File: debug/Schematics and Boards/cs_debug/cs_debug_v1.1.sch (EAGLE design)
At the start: 241 parts, among them J1 J-JTAG-CORTEX_SMD, J19 Solar, J2 J-JTAG-CORTEX_SMD, J3 J-JTAG-CORTEX-NEEDLE6-LEGS, J4 J-SERIAL-PORT, J5 J-WURTH-USBC, Q10 2N7002P, Q3 FDN340P, Q4 2N7002P, Q5 FDN340P, Q6 2N7002P, Q7 FDN340P, Q8 2N7002P, Q9 FDN340P, U1 AP2120N-3.3TRG1, U10 OPA357AIDBVTG4, U11 DAC7574IDGS, U12 MCP73871T-2CCI/ML, U13 USB2412-DZK, U14 INA225AIDGK, U15 OPA357AIDBVTG4, U2 TLV1117LV33DCYR, U5 INA225AIDGK, U6 OPA357AIDBVTG4, U7 INA225AIDGK, U8 OPA357AIDBVTG4, U9 INA225AIDGK, Y1 EPSON_TSX-3225_24.0000MF10Z-C3, Y101 32.768kHz, Y102 12mHz-12pF-K7

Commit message: Schematic updates and component placement for debug placement
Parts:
- removed J.USB.DBG, J.USB.MN: USBABSMTDIP, ZX62D-AB-5P8:USBABSMTDIP
- removed J2: J-JTAG-CORTEX_SMD, Connectors:J-JTAG-CORTEX_SMD
- removed JP.HUB.VDD, JP.IP.CORE, JP.IP.RST, JP.UART.RX.IP, JP.UART.TX.IP, JP.USB.USART, JP.USBC.VBUS: JUMPER-SMT_2_NC_PASTE_NO-SILK, Connectors:JUMPER-SMT_2_NC_PASTE_NO-SILK
- removed JP.USB.DBG, JP.USBC: JUMPER-SMT_2_NO_PASTEFREE, Connectors:JUMPER-SMT_2_NO_PASTEFREE
- removed JP.USB.DDN, JP.USB.DDP, JP.USB.MDN, JP.USB.MDP, JP.USB.VBUSP, JP.VREG.SEL: JUMPER-SMT_3_1-NC_PASTE_NO-SILK, Connectors:JUMPER-SMT_3_1-NC_PASTE_NO-SILK
- removed J_DBG_TO_MAIN_HDR: HIROSE-DF40_30-PIN_CONNECTORS-HEADER, Connectors:HIROSE-DF40_30-PIN_CONNECTORS-HEADER
- removed L2: DLP11SN900HL2L, Inductors:DLP11SN900HL2L
- removed M.D.DA.VO, M.D.OA.EN, M.D.OA.N, M.D.OA.P, M.D.OA.VO, M.D.SDN, M.D.VN, M.D.VOI, M.P.DA.VO, M.P.OA.EN, M.P.OA.N, M.P.OA.P, M.P.OA.VO, M.P.SDN, M.P.VN, M.P.VOI, M.S.DA.VO, M.S.OA.EN, M.S.OA.N, M.S.OA.P, M.S.OA.VO, M.S.SDN, M.S.VN, M.S.VOI, M.T.DA.VO, M.T.OA.EN, M.T.OA.N, M.T.OA.P, M.T.OA.VO, M.T.SDN, M.T.VN, M.T.VOI: TPTP10SQ, TestPoints:TPTP10SQ
- removed R44, R45, R51, R52: 10k, Resistors:R-0402
- removed R50: 100k, Resistors:R-0402
- removed VR1, VR2, VR5, VR6, VR7, VR8: VARISTOR, Diodes:VARISTOR
- added C4, C5, C6: 0.1u, Capacitors:C-0402
- added C57: 1u, Capacitors:C-0402
- added CHRG, HUB.VDD, USB.VSRC: JUMPER-SMT_2_NC_PASTE_NO-SILK, Connectors:JUMPER-SMT_2_NC_PASTE_NO-SILK
- added D0DAO, D0OFF, D0OPN, D0OPO, D0OPP, D1DAO, D1OFF, D1OPN, D1OPO, D1OPP, PDAO, POPN, POPO, POPP, PROFF, SDAO, SOPN, SOPO, SOPP, STOFF: TPSTP10SQ, TestPoints:TPSTP10SQ
- added HUB.HS, HUB.SUSP, LOW_BAT, PG, STAT2: (no value), Diodes:LEDCHIPLED_0603
- added JP1: (no value), Connectors:J-HEADER-1X12
- added R10: 270, Resistors:R-0402
- added R9: 750, Resistors:R-0402
- added U204: LOADSWITCH-MIC94164, Switches:LOADSWITCH-MIC94164
- added U3: ESD122DMYR, Diodes:ESD122DMYR
- added VREG.SEL: JUMPER-SMT_3_1-NC_PASTE_NO-SILK, Connectors:JUMPER-SMT_3_1-NC_PASTE_NO-SILK
- C10, C13, C7: value 270nF -> 0.1u; device Capacitors:C-0603 -> Capacitors:C-0402; MPN C0603C274K8PACTU -> C0402C104K4RAC7411; PART_NO C0603C274K8PACTU -> C0402C104K4RAC7411; TC X5R -> (none)
- C20: value 270nF -> 10u; device Capacitors:C-0603 -> Capacitors:C-1206; MPN C0603C274K8PACTU -> C1206C476M8PACTU; PART_NO C0603C274K8PACTU -> C1206C476M8PACTU; TOL 0.5pF -> 20%
- D2: value BGX50A -> MBR120VLSFT3GOSCT-ND; device Diodes:BGX50A -> adafruit:DIODESOD-123; MPN (none) -> MBR120VLSFT3G; PART_NO (none) -> MBR120VLSFT3G
- J3: value J-JTAG-CORTEX-NEEDLE6-LEGS -> HIROSE-DF40_50-PIN_CONNECTORS-HEADER; device Connectors:J-JTAG-CORTEX-NEEDLE6-LEGS -> Connectors:HIROSE-DF40_50-PIN_CONNECTORS-HEADER
- JP.UART.VCC: value JUMPER-SMT_2_NC_PASTE_NO-SILK -> JUMPER-SMT_2_NO_PASTEFREE; device Connectors:JUMPER-SMT_2_NC_PASTE_NO-SILK -> Connectors:JUMPER-SMT_2_NO_PASTEFREE
- R2, R3: value 100k -> 1.5k; MPN ERJ-2GEJ104X -> ERJ-2GEJ152X; PART_NO ERJ-2GEJ104X -> ERJ-2GEJ152X
- R6: value 100k -> 1.15k; MPN ERJ-2GEJ104X -> ERJ-2RKF1151X; PART_NO ERJ-2GEJ104X -> ERJ-2RKF1151X; TOL (none) -> 1%
- R7: value 1M -> 100k; MPN ERJ-U02J105X -> ERJ-2GEJ104X; PART_NO ERJ-U02J105X -> ERJ-2GEJ104X
- S.ERASE, S.NRST: device Switches:SW_EVQ-P7L01P_SPST_RA -> Switches:MOMENTARY-SWITCH-SPST-SMD-5.2MM
- Y102: value 12mHz-12pF-K7 -> 12MHz-12pF-K7
- renumbered 3V3.IPROC to IP.3V3, JP.CHRG.MAIN to MN.CHRG, JP.EN.VMEAS to REGMEAS, JP.EN.VPROC to REGPROC, JP.EXT.PWR to EXT.SRC, JP.IP.ANA to IP.ANA, JP.IP.AREF to IP.AREF, JP.IP.OUT to IP.OUT, JP.IP.PLL to IP.PLL, JP.IP.UTMI to IP.UTMI, JP.IP.VDDIO to IP.VDDIO, JP.P.DTR to VP.DTR0, JP.P.PROC to VP.PRC, JP.P.STOR to VP.DTR1, JP.P.TEMP to VP.STOR, JP.UART.RX to MN.UART.RX, JP.UART.TX to MN.UART.TX, JP.VDD.MAIN to MN.VDD
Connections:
- net CM_DIFFAMP_N2 renamed CM_DTR1_DIFFAMP_N
- net CM_DIFFAMP_P2 renamed CM_DTR1_DIFFAMP_P
- net CM_DTR_DIFFAMP_GAIN0 renamed CM_DTR0_DIFFAMP_GAIN0
- net CM_DTR_DIFFAMP_GAIN1 renamed CM_DTR0_DIFFAMP_GAIN1
- net CM_DTR_V_SENSE_P renamed CM_DTR0_V_SENSE_P
- net CM_STORAGE_DIFFAMP_GAIN0 renamed CM_DTR1_DIFFAMP_GAIN0
- net CM_STORAGE_DIFFAMP_GAIN1 renamed CM_DTR1_DIFFAMP_GAIN1
- net CM_STORAGE_V_SENSE_P renamed CM_DTR1_V_SENSE_P
- net CM_TEMP_DIFFAMP_GAIN0 renamed CM_STOR_DIFFAMP_GAIN0
- net CM_TEMP_DIFFAMP_GAIN1 renamed CM_STOR_DIFFAMP_GAIN1
- net CM_TEMP_V_SENSE_P renamed CM_STOR_V_SENSE_P
- removed net CM_DIFFAMP_N1: C20.1, R58.2, U14.IN-
- removed net CM_DIFFAMP_N3: C10.1, R31.2, U7.IN-
- removed net CM_DIFFAMP_P1: C20.2, R59.2, U14.IN+
- removed net CM_DIFFAMP_P3: C10.2, R32.2, U7.IN+
- removed net CM_DTR_DCBIAS_SHUTDOWN: M.D.SDN.TP, Q8.GATE, R30.1, U_INSTR_PROC.PD2
- removed net CM_DTR_DIFFAMP_OUT: M.D.DA.VO.TP, U7.OUT, U_INSTR_PROC.PA6
- removed net CM_DTR_V_OFFSET_IN: M.D.VOI.TP, R25.1, U11.VOUTB
- removed net CM_DTR_V_SENSE_N: J_DBG_TO_MAIN_HDR.16, M.D.VN.TP, Q7.D, R26.1
- removed net CM_OPAMP_ENABLE1: M.T.OA.EN.TP, Q10.DRAIN, Q9.G, R54.1, U15.ENABLE
- removed net CM_OPAMP_ENABLE2: M.S.OA.EN.TP, Q5.G, Q6.DRAIN, R34.1, U10.ENABLE
- removed net CM_OPAMP_ENABLE3: M.D.OA.EN.TP, Q7.G, Q8.DRAIN, R27.1, U8.ENABLE
- removed net CM_OPAMP_N1: M.T.OA.N.TP, R55.1, R56.2, U15.IN-
- removed net CM_OPAMP_N2: M.S.OA.N.TP, R35.1, R36.2, U10.IN-
- removed net CM_OPAMP_N3: M.D.OA.N.TP, R28.1, R29.2, U8.IN-
- removed net CM_OPAMP_OUT1: M.T.OA.VO.TP, Q9.S, R55.2, R58.1, U15.OUT
- removed net CM_OPAMP_OUT2: M.S.OA.VO.TP, Q5.S, R35.2, R38.1, U10.OUT
- removed net CM_OPAMP_OUT3: M.D.OA.VO.TP, Q7.S, R28.2, R31.1, U8.OUT
- removed net CM_OPAMP_P2: M.S.OA.P.TP, R24.2, R33.2, U10.IN+
- removed net CM_STORAGE_DCBIAS_SHUTDOWN: M.S.SDN.TP, Q6.GATE, R37.1, U_INSTR_PROC.PD1
- removed net CM_STORAGE_DIFFAMP_OUT: M.S.DA.VO.TP, U9.OUT, U_INSTR_PROC.PA4
- removed net CM_STORAGE_V_OFFSET_IN: M.S.VOI.TP, R24.1, U11.VOUTC
- removed net CM_STORAGE_V_SENSE_N: J_DBG_TO_MAIN_HDR.18, M.S.VN.TP, Q5.D, R33.1
- removed net CM_TEMP_DCBIAS_SHUTDOWN: M.T.SDN.TP, Q10.GATE, R57.1, U_INSTR_PROC.PD0
- removed net CM_TEMP_DIFFAMP_OUT: M.T.DA.VO.TP, U14.OUT, U_INSTR_PROC.PA3
- removed net CM_TEMP_V_OFFSET_IN: M.T.VOI.TP, R40.1, U11.VOUTD
- removed net CM_TEMP_V_SENSE_N: J_DBG_TO_MAIN_HDR.20, M.T.VN.TP, Q9.D, R53.1
- removed net HUB_INSTR_PROC_USB_D_N: JP.USB.DDN.3, U13.USBDM_DN2
- removed net HUB_INSTR_PROC_USB_D_P: JP.USB.DDP.3, U13.USBDP_DN2
- removed net HUB_MAIN_USB_DATA_N: JP.USB.MDN.3, U13.USBDM_DN1
- removed net HUB_MAIN_USB_DATA_P: JP.USB.MDP.3, U13.USBDP_DN1
- removed net INSTR_PROC_JTAG_TCK/SWCLK: J2.SWDCLK/TCK, J3.SWCLK, R3.1, U_INSTR_PROC.PB28
- removed net INSTR_PROC_JTAG_TDI: J2.NC/TDI, R6.1, U_INSTR_PROC.PB29
- removed net INSTR_PROC_JTAG_TDO/SWO: J2.SWO/TDO, J3.SWO, U_INSTR_PROC.PB30
- removed net INSTR_PROC_JTAG_TMS/SWDIO: J2.SWDIO/TMS, J3.SWDIO, R2.1, U_INSTR_PROC.PB31
- removed net INSTR_PROC_NRESET: J2.!RESET, J3.NRESET, JP.IP.RST.1
- removed net MAIN_TRACE_CLK/GPIO4: J_DBG_TO_MAIN_HDR.26, U_INSTR_PROC.PC15
- removed net MAIN_TRACE_D0/GPIO6: J_DBG_TO_MAIN_HDR.23, U_INSTR_PROC.PB1
- removed net MAIN_TRACE_D1/GPIO7: J_DBG_TO_MAIN_HDR.25, U_INSTR_PROC.PB2
- removed net MAIN_TRACE_D2/GPIO8: J_DBG_TO_MAIN_HDR.27
- removed net MAIN_TRACE_D3/GPIO9: J_DBG_TO_MAIN_HDR.29
- removed net MAIN_TRACE_SWO/GPIO5: J_DBG_TO_MAIN_HDR.28, U_INSTR_PROC.PB0
- removed net USB_BKUP_DBG_D_N: J.USB.DBG.D-, JP.USB.DDN.1, VR5.1
- removed net USB_BKUP_DBG_D_P: J.USB.DBG.D+, JP.USB.DDP.1, VR2.1
- removed net USB_BKUP_DBG_OTGID: J.USB.DBG.USBID, VR1.1
- removed net USB_BKUP_DBG_VBUS: J.USB.DBG.VBUS, JP.USB.DBG.2, JP.USB.VBUSP.1
- removed net USB_BKUP_MAIN_D_N: J.USB.MN.D-, JP.USB.MDP.1, VR8.1
- removed net USB_BKUP_MAIN_D_P: J.USB.MN.D+, JP.USB.MDN.1, VR7.1
- removed net USB_BKUP_MAIN_OTGID: J.USB.MN.USBID, VR6.1
- removed net USB_BKUP_MAIN_VBUS: J.USB.MN.VBUS, JP.USBC.2
- removed net USB_CONN_D_N: D2.AC1, J5_CONNECTOR.DP1, J5_CONNECTOR.DP2, L2.3, VR3.1
- removed net USB_CONN_D_P: D2.AC2, J5_CONNECTOR.DN1, J5_CONNECTOR.DN2, L2.2, VR4.1
- removed net VDDOUT_1: JP.IP.CORE.1, U_INSTR_PROC.VDDCORE1, U_INSTR_PROC.VDDCORE2, U_INSTR_PROC.VDDCORE3, U_INSTR_PROC.VDDCORE4, U_INSTR_PROC.VDDCORE5
- new net +3V3_INSTR_PROC: HUB.VDD.1
- new net CM_DTR0_DCBIAS_SHUTDOWN: Q8.GATE, R30.1, U_INSTR_PROC.PD2
- new net CM_DTR0_DIFFAMP_N: C7.1, R31.2, U7.IN-
- new net CM_DTR0_DIFFAMP_OUT: D0DAO.PP, U7.OUT, U_INSTR_PROC.PA6
- new net CM_DTR0_DIFFAMP_P3: C7.2, R32.2, U7.IN+
- new net CM_DTR0_OPAMP_ENABLE: Q7.G, Q8.DRAIN, R27.1, U8.ENABLE
- new net CM_DTR0_OPAMP_N: D0OPN.PP, R28.1, R29.2, U8.IN-
- new net CM_DTR0_OPAMP_OUT: D0OPO.PP, Q7.S, R28.2, R31.1, U8.OUT
- new net CM_DTR0_V_OFFSET_IN: D0OFF.PP, R25.1, U11.VOUTB
- new net CM_DTR0_V_SENSE_N: J3.18, Q7.D, R26.1
- new net CM_DTR1_DCBIAS_SHUTDOWN: Q6.GATE, R37.1, U_INSTR_PROC.PD1
- new net CM_DTR1_DIFFAMP_OUT: D1DAO.PP, U9.OUT, U_INSTR_PROC.PA4
- new net CM_DTR1_OPAMP_N: D1OPN.PP, R35.1, R36.2, U10.IN-
- new net CM_DTR1_OPAMP_OUT: D1OPO.PP, Q5.S, R35.2, R38.1, U10.OUT
- new net CM_DTR1_OPAMP_P: D1OPP.PP, R24.2, R33.2, U10.IN+
- new net CM_DTR1_V_OFFSET_IN: D1OFF.PP, R24.1, U11.VOUTC
- new net CM_DTR1_V_SENSE_N: J3.20, Q5.D, R33.1
- new net CM_DTR_OPAMP_ENABLE: Q5.G, Q6.DRAIN, R34.1, U10.ENABLE
- new net CM_STORV_SENSE_N: J3.22
- new net CM_STOR_DCBIAS_SHUTDOWN: Q10.GATE, R57.1, U_INSTR_PROC.PD0
- new net CM_STOR_DIFFAMP_N1: C10.1, R58.2, U14.IN-
- new net CM_STOR_DIFFAMP_OUT: SDAO.PP, U14.OUT, U_INSTR_PROC.PA3
- new net CM_STOR_DIFFAMP_P1: C10.2, R59.2, U14.IN+
- new net CM_STOR_OPAMP_ENABLE: Q10.DRAIN, Q9.G, R54.1, U15.ENABLE
- new net CM_STOR_OPAMP_N: R55.1, R56.2, SOPN.PP, U15.IN-
- new net CM_STOR_OPAMP_OUT: Q9.S, R55.2, R58.1, SOPO.PP, U15.OUT
- new net CM_STOR_V_OFFSET_IN: R40.1, STOFF.PP, U11.VOUTD
- new net CM_STOR_V_SENSE_N: Q9.D, R53.1
- new net MAIN_GPIO10: J3.40, U_INSTR_PROC.PB1
- new net MAIN_GPIO11: J3.38, U_INSTR_PROC.PB2
- new net MAIN_GPIO4/SERCOM_P0: J3.30, JP1.2
- new net MAIN_GPIO5/SERCOM_P1: J3.32, JP1.3
- new net MAIN_GPIO6/SERCOM_P2: J3.34, JP1.4
- new net MAIN_GPIO7/SERCOM_P3: J3.36, JP1.5
- new net MAIN_GPIO8: J3.44, U_INSTR_PROC.PC15
- new net MAIN_GPIO9: J3.42, U_INSTR_PROC.PB0
- new net MAIN_TRACE_CLK/GPIO17: J3.23, JP1.11
- new net MAIN_TRACE_D0/GPIO13: J3.15, JP1.7
- new net MAIN_TRACE_D1/GPIO14: J3.17, JP1.8
- new net MAIN_TRACE_D2/GPIO15: J3.19, JP1.9
- new net MAIN_TRACE_D3/GPIO16: J3.21, JP1.10
- new net MAIN_TRACE_SWO/GPIO12: J3.13, JP1.6
- new net N$12: R2.1, U12.STAT1/!LBO
- new net N$17: C5.1, U13.PLLFILT
- new net N$18: R3.2, STAT2.C
- new net N$19: PG.C, R6.2
- new net N$20: R6.1, U12.!PG
- new net N$22: HUB.SUSP.A, R9.1
- new net N$23: HUB.HS.A, R10.1
- new net N$24: CHRG.1, R201.2, U12.!TE, U12.CE, U12.IN, U12.PROG2, U12.SEL
- new net VUSB_DIODE: D2.C, USB.VSRC.1
- net 3V3_INSTR_MEAS: now also JP1.1
- net 3V3_INSTR_PROC: no longer C49.1, C50.1, C51.1, C52.1, C53.1, C54.1, J2.VCC, J3.VTREF, JP.HUB.VDD.1, R2.2, R3.2, R44.2, R45.2, R51.2, R52.2, R6.2
- net CM_DIFFAMP_N4: now also C6.1; no longer C7.1
- net CM_DIFFAMP_P4: now also C6.2; no longer C7.2
- net CM_OPAMP_ENABLE4: no longer M.P.OA.EN.TP
- net CM_OPAMP_N4: now also POPN.PP; no longer M.P.OA.N.TP
- net CM_OPAMP_OUT4: now also POPO.PP; no longer M.P.OA.VO.TP
- net CM_OPAMP_P1: now also SOPP.PP; no longer M.T.OA.P.TP
- net CM_OPAMP_P3: now also D0OPP.PP; no longer M.D.OA.P.TP
- net CM_OPAMP_P4: now also POPP.PP; no longer M.P.OA.P.TP
- net CM_PROC_DCBIAS_SHUTDOWN: no longer M.P.SDN.TP
- net CM_PROC_DIFFAMP_OUT: now also PDAO.PP; no longer M.P.DA.VO.TP
- net CM_PROC_V_OFFSET_IN: now also PROFF.PP; no longer M.P.VOI.TP
- net CM_PROC_V_SENSE_N: now also J3.16; no longer J_DBG_TO_MAIN_HDR.14, M.P.VN.TP
- net DGND: now also C20.2, C4.2, C5.2, C57.2, HUB.HS.C, HUB.SUSP.C, J3.1, J3.3, J3.5, J3.7, JP1.12, R7.1, U204.GND, U3.GND; no longer D2.-, J.USB.DBG.GND, J.USB.DBG.SHIELD, J.USB.MN.GND, J.USB.MN.SHIELD, J2.GND@3, J2.GND@5, J2.GNDDTCT, J3.GND, J_DBG_TO_MAIN_HDR.1, J_DBG_TO_MAIN_HDR.3, J_DBG_TO_MAIN_HDR.5, R50.1, VR1.2, VR2.2, VR5.2, VR6.2, VR7.2, VR8.2
- net INSTR_PROC_NRESET_SW: no longer JP.IP.RST.2
- net INSTR_PROC_USB_D_N: now also U13.USBDM_DN1; no longer JP.USB.DDN.2
- net INSTR_PROC_USB_D_P: now also U13.USBDP_DN1; no longer JP.USB.DDP.2
- net MAIN_GPIO0: now also J3.31; no longer J_DBG_TO_MAIN_HDR.7
- net MAIN_GPIO1: now also J3.29; no longer J_DBG_TO_MAIN_HDR.9
- net MAIN_GPIO2: now also J3.27; no longer J_DBG_TO_MAIN_HDR.11
- net MAIN_GPIO3: now also J3.25; no longer J_DBG_TO_MAIN_HDR.13
- net MAIN_NRESET: now also J3.24; no longer J_DBG_TO_MAIN_HDR.30
- net MAIN_SWD_SWCLK: now also J3.28; no longer J_DBG_TO_MAIN_HDR.19
- net MAIN_SWD_SWDIO: now also J3.26; no longer J_DBG_TO_MAIN_HDR.21
- net MAIN_USART_RX: now also J3.9; no longer JP.UART.TX.IP.1, J_DBG_TO_MAIN_HDR.17
- net MAIN_USART_TX: now also J3.11; no longer JP.UART.RX.IP.1, JP.USB.USART.2, J_DBG_TO_MAIN_HDR.15
- net MAIN_USB_DATA_N: now also J3.49, U13.USBDM_DN2; no longer JP.USB.MDN.2, J_DBG_TO_MAIN_HDR.22
- net MAIN_USB_DATA_P: now also J3.47, U13.USBDP_DN2; no longer JP.USB.MDP.2, J_DBG_TO_MAIN_HDR.24
- net N$14: now also R3.1, U12.STAT2; no longer R45.1, U13.PRTPWR1
- net N$16: now also C4.1, U13.CRFILT; no longer R44.1, U13.PRTPWR2
- net N$3: now also S201.P, U204.ENABLE; no longer JP.UART.TX.IP.2, U_INSTR_PROC.PD5
- net N$5: now also LOW_BAT.C, R2.2; no longer JP.UART.RX.IP.2, U_INSTR_PROC.PD4
- net N$6: now also C20.1, S201.S, U204.VIN; no longer S201.P
- net UCTX_DBGRX: no longer JP.USB.USART.1
- net USBC_VBUS: now also D2.A; no longer D2.+, JP.USB.VBUSP.3, JP.USBC.VBUS.1
- net USB_D_N: now also J5_CONNECTOR.DN1, J5_CONNECTOR.DN2, U3.IO2, VR3.1; no longer L2.4
- net USB_D_P: now also J5_CONNECTOR.DP1, J5_CONNECTOR.DP2, U3.IO1, VR4.1; no longer L2.1
- net USB_HS_IND: now also R10.2; no longer R50.2
- net USB_HUB_VDD: now also C49.1, C50.1, C51.1, C52.1, C53.1, C54.1, HUB.VDD.2; no longer JP.HUB.VDD.2
- net USB_NONRMV0: now also R9.2; no longer R51.1
- net USB_NONRMV1: now also R7.2; no longer R52.1
- net USB_VBUS_IPROC: no longer JP.USB.VBUSP.2
- net USB_XIN: no longer R7.2
- net USB_XOUT: no longer R7.1
- net VCHRG_OUT: now also VREG.SEL.3; no longer JP.VREG.SEL.3
- net VDDOUT: now also U_INSTR_PROC.VDDCORE1, U_INSTR_PROC.VDDCORE2, U_INSTR_PROC.VDDCORE3, U_INSTR_PROC.VDDCORE4, U_INSTR_PROC.VDDCORE5; no longer JP.IP.CORE.2
- net VDD_TO_MAIN: now also J3.2, J3.4, J3.6; no longer J_DBG_TO_MAIN_HDR.2, J_DBG_TO_MAIN_HDR.4
- net VREG_IN: now also VREG.SEL.2; no longer JP.VREG.SEL.2
- net VSRC: now also USB.VSRC.2; no longer JP.USB.DBG.1, JP.USBC.1, JP.USBC.VBUS.2
- net VSRC_RAW: now also C57.1, CHRG.2, LOW_BAT.A, PG.A, STAT2.A, U204.VOUT, VREG.SEL.1; no longer JP.VREG.SEL.1, R201.2, S201.S, U12.!TE, U12.CE, U12.IN, U12.PROG2, U12.SEL
- net V_BATT_MAIN: now also J3.10, J3.12, J3.8; no longer J_DBG_TO_MAIN_HDR.10, J_DBG_TO_MAIN_HDR.6, J_DBG_TO_MAIN_HDR.8
- net V_SENSE_P: now also J3.14; no longer J_DBG_TO_MAIN_HDR.12
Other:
- note added: "Daughter Board High-Side Current Monitor 0"
- note added: "Daughter High-Side Current Monitor 1"
- note added: "GPIO Expansion"
- note added: "Green"
- note added: "Orange"
- note added: "Red"
- note added: "Storage/FLASH High-Side Current Monitor"
- note added: "Yellow"
- note removed: "Add DLP11SN900SL2 and BGX50A"
- note removed: "Both debug connector options in case dev is missing a cable. Tag-connect is missing TDI, so it may not work"
- note removed: "Daughter Board High-Side Current Monitor"
- note removed: "Instrumentation Processor Debugging"
- note removed: "Storage High-Side Current Monitor"
- note removed: "Temp High-Side Current Monitor"
- note removed: "USB Micro Connectors (backup for hub)"
- moved on the sheet: C10, C208, C7, D1, L1, R48, R7, S201

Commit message: Finished schematic revision for main, debug boards.
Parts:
- C.PHAT: value 10u -> 47u
- renumbered C20 to C.PHAT, J4 to J.FTDI, R1 to R.GND, U_INSTR_PROC to U.IP
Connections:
- net N$3 renamed VREG.SW.EN
- net N$6 renamed VSRC_SW
- removed net USB_VBUS_IPROC: U.IP.VBUS
- net USBC_VBUS: now also U.IP.VBUS
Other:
- note added: "GPIO Expansion for main board"
- note added: "Monitor 0 is nominally for measuring current of the entire stack of daughter boards, but can be switched to instead measure the current of a particular component or subsystem."
- note removed: "Connection questionable"
- note removed: "GPIO Expansion"
- note removed: "pull-up for power pins; hub should not shutdown other devices"
- moved on the sheet: HUB.HS, JP1, PG, STAT2

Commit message: Route differential USB signals
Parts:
- added R1: 51k, Resistors:R-0402
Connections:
- removed net N$22: HUB.SUSP.A, R9.1
- new net N$3: HUB.SUSP.C, R9.1
- net 3V3_INSTR_PROC: now also HUB.SUSP.A, R1.1
- net DGND: no longer HUB.SUSP.C
- net USB_NONRMV0: now also R1.2
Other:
- note added: "Mark port 2 as removeable"
- moved on the sheet: C4, C5, HUB.SUSP, R48, R7, R9

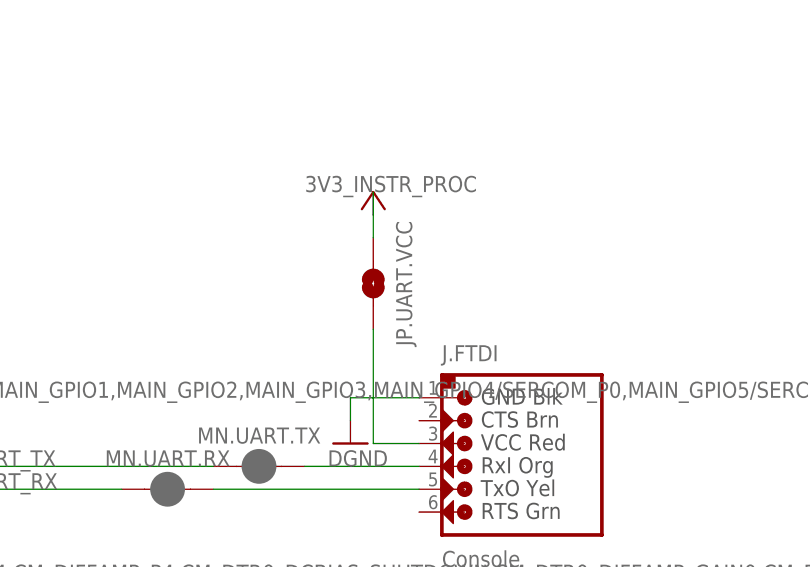
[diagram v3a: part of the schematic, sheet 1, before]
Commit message: Edit silk and documentation layers for pick-and-place assembly
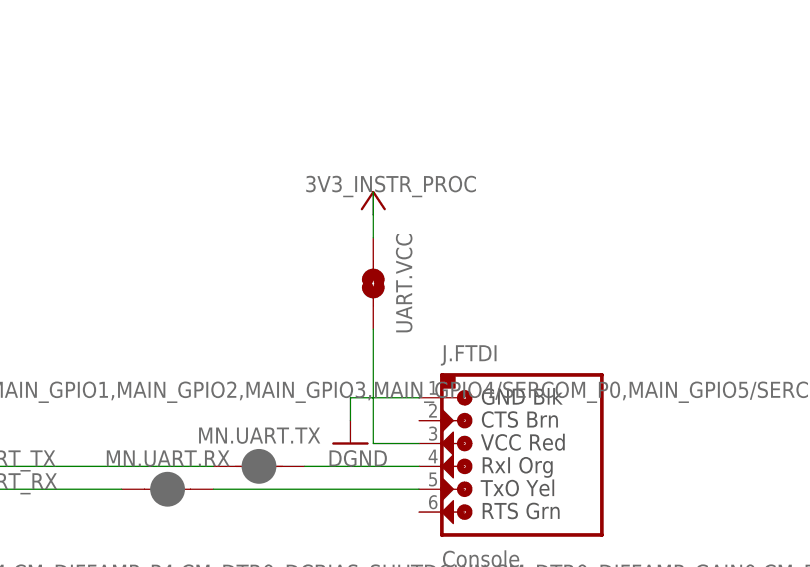
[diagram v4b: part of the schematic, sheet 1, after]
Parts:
- renumbered JP.UART.VCC to UART.VCC
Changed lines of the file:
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@@
 </part>
 <part name="SUPPLY25" library="Supplies" deviceset="+3V3" device=""/>
-<part name="JP.UART.VCC" library="Connectors" deviceset="JUMPER-SMT_2_NO_PASTEFREE" device=""/>
+<part name="UART.VCC" library="Connectors" deviceset="JUMPER-SMT_2_NO_PASTEFREE" device=""/>
 <part name="C46" library="Capacitors" deviceset="C-" device="0603" value="2.2uF">
 <attribute name="MPN" value="C0603C225K8RACTU"/>
@@
 </instance>
 <instance part="SUPPLY25" gate="G$1" x="523.24" y="236.22" smashed="yes"/>
-<instance part="JP.UART.VCC" gate="G$1" x="523.24" y="226.06" smashed="yes" rot="R270">
+<instance part="UART.VCC" gate="G$1" x="523.24" y="226.06" smashed="yes" rot="R270">
 <attribute name="NAME" x="525.78" y="226.06" size="1.778" layer="95" font="vector" rot="R270" align="bottom-center"/>
 </instance>
@@
 <label x="515.62" y="236.22" size="1.778" layer="95"/>
 <pinref part="SUPPLY25" gate="G$1" pin="+3V3"/>
-<pinref part="JP.UART.VCC" gate="G$1" pin="1"/>
+<pinref part="UART.VCC" gate="G$1" pin="1"/>
 <wire x1="523.24" y1="231.14" x2="523.24" y2="233.68" width="0.1524" layer="91"/>
 </segment>
@@
 <net name="N$11" class="0">
 <segment>
-<pinref part="JP.UART.VCC" gate="G$1" pin="2"/>
+<pinref part="UART.VCC" gate="G$1" pin="2"/>
 <pinref part="J.FTDI" gate="J$1" pin="VCC-I"/>
 <wire x1="523.24" y1="220.98" x2="523.24" y2="208.28" width="0.1524" layer="91"/>

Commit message: Route minimal analog signals under ground bridge, add near ground plugs
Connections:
- removed net CM_STORV_SENSE_N: J3.22
- net CM_STOR_V_SENSE_N: now also J3.22
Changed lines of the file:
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@@
 </instances>
 <busses>
-<bus name="POWER_SENSING:CM_DIFFAMP_N4,CM_DIFFAMP_P4,CM_DTR0_DCBIAS_SHUTDOWN,CM_DTR0_DIFFAMP_GAIN0,CM_DTR0_DIFFAMP_GAIN1,CM_DTR0_DIFFAMP_N,CM_DTR0_DIFFAMP_OUT,CM_DTR0_DIFFAMP_P3,CM_DTR0_OPAMP_ENABLE,CM_DTR0_OPAMP_N,CM_DTR0_OPAMP_OUT,CM_DTR0_V_OFFSET_IN,CM_DTR0_V_SENSE_N,CM_DTR0_V_SENSE_P,CM_DTR1_DCBIAS_SHUTDOWN,CM_DTR1_DIFFAMP_GAIN0,CM_DTR1_DIFFAMP_GAIN1,CM_DTR1_DIFFAMP_N,CM_DTR1_DIFFAMP_OUT,CM_DTR1_DIFFAMP_P,CM_DTR1_OPAMP_N,CM_DTR1_OPAMP_OUT,CM_DTR1_OPAMP_P,CM_DTR1_V_OFFSET_IN,CM_DTR1_V_SENSE_N,CM_DTR1_V_SENSE_P,CM_DTR_OPAMP_ENABLE,CM_OPAMP_ENABLE4,CM_OPAMP_N4,CM_OPAMP_OUT4,CM_OPAMP_P1,CM_OPAMP_P3,CM_OPAMP_P4,CM_PROC_DCBIAS_SHUTDOWN,CM_PROC_DIFFAMP_GAIN0,CM_PROC_DIFFAMP_GAIN1,CM_PROC_DIFFAMP_OUT,CM_PROC_V_OFFSET_IN,CM_PROC_V_SENSE_N,CM_PROC_V_SENSE_P,CM_STOR_DCBIAS_SHUTDOWN,CM_STOR_DIFFAMP_GAIN0,CM_STOR_DIFFAMP_GAIN1,CM_STOR_DIFFAMP_N1,CM_STOR_DIFFAMP_OUT,CM_STOR_DIFFAMP_P1,CM_STOR_OPAMP_ENABLE,CM_STOR_OPAMP_N,CM_STOR_OPAMP_OUT,CM_STOR_V_OFFSET_IN,CM_STORV_SENSE_N,CM_STOR_V_SENSE_N,CM_STOR_V_SENSE_P,V_SENSE_P">
+<bus name="POWER_SENSING:CM_DIFFAMP_N4,CM_DIFFAMP_P4,CM_DTR0_DCBIAS_SHUTDOWN,CM_DTR0_DIFFAMP_GAIN0,CM_DTR0_DIFFAMP_GAIN1,CM_DTR0_DIFFAMP_N,CM_DTR0_DIFFAMP_OUT,CM_DTR0_DIFFAMP_P3,CM_DTR0_OPAMP_ENABLE,CM_DTR0_OPAMP_N,CM_DTR0_OPAMP_OUT,CM_DTR0_V_OFFSET_IN,CM_DTR0_V_SENSE_N,CM_DTR0_V_SENSE_P,CM_DTR1_DCBIAS_SHUTDOWN,CM_DTR1_DIFFAMP_GAIN0,CM_DTR1_DIFFAMP_GAIN1,CM_DTR1_DIFFAMP_N,CM_DTR1_DIFFAMP_OUT,CM_DTR1_DIFFAMP_P,CM_DTR1_OPAMP_N,CM_DTR1_OPAMP_OUT,CM_DTR1_OPAMP_P,CM_DTR1_V_OFFSET_IN,CM_DTR1_V_SENSE_N,CM_DTR1_V_SENSE_P,CM_DTR_OPAMP_ENABLE,CM_OPAMP_ENABLE4,CM_OPAMP_N4,CM_OPAMP_OUT4,CM_OPAMP_P1,CM_OPAMP_P3,CM_OPAMP_P4,CM_PROC_DCBIAS_SHUTDOWN,CM_PROC_DIFFAMP_GAIN0,CM_PROC_DIFFAMP_GAIN1,CM_PROC_DIFFAMP_OUT,CM_PROC_V_OFFSET_IN,CM_PROC_V_SENSE_N,CM_PROC_V_SENSE_P,CM_STOR_DCBIAS_SHUTDOWN,CM_STOR_DIFFAMP_GAIN0,CM_STOR_DIFFAMP_GAIN1,CM_STOR_DIFFAMP_N1,CM_STOR_DIFFAMP_OUT,CM_STOR_DIFFAMP_P1,CM_STOR_OPAMP_ENABLE,CM_STOR_OPAMP_N,CM_STOR_OPAMP_OUT,CM_STOR_V_OFFSET_IN,CM_STOR_V_SENSE_N,CM_STOR_V_SENSE_P,V_SENSE_P">
 <segment>
 <wire x1="137.16" y1="172.72" x2="137.16" y2="7.62" width="0.762" layer="92"/>
@@
 </segment>
 </bus>
-<bus name="POWER_SENSING:CM_DIFFAMP_N4,CM_DIFFAMP_P4,CM_DTR0_DCBIAS_SHUTDOWN,CM_DTR0_DIFFAMP_GAIN0,CM_DTR0_DIFFAMP_GAIN1,CM_DTR0_DIFFAMP_N,CM_DTR0_DIFFAMP_OUT,CM_DTR0_DIFFAMP_P3,CM_DTR0_OPAMP_ENABLE,CM_DTR0_OPAMP_N,CM_DTR0_OPAMP_OUT,CM_DTR0_V_OFFSET_IN,CM_DTR0_V_SENSE_N,CM_DTR0_V_SENSE_P,CM_DTR1_DCBIAS_SHUTDOWN,CM_DTR1_DIFFAMP_GAIN0,CM_DTR1_DIFFAMP_GAIN1,CM_DTR1_DIFFAMP_N,CM_DTR1_DIFFAMP_OUT,CM_DTR1_DIFFAMP_P,CM_DTR1_OPAMP_N,CM_DTR1_OPAMP_OUT,CM_DTR1_OPAMP_P,CM_DTR1_V_OFFSET_IN,CM_DTR1_V_SENSE_N,CM_DTR1_V_SENSE_P,CM_DTR_OPAMP_ENABLE,CM_OPAMP_ENABLE4,CM_OPAMP_N4,CM_OPAMP_OUT4,CM_OPAMP_P1,CM_OPAMP_P3,CM_OPAMP_P4,CM_PROC_DCBIAS_SHUTDOWN,CM_PROC_DIFFAMP_GAIN0,CM_PROC_DIFFAMP_GAIN1,CM_PROC_DIFFAMP_OUT,CM_PROC_V_OFFSET_IN,CM_PROC_V_SENSE_N,CM_PROC_V_SENSE_P,CM_STOR_DCBIAS_SHUTDOWN,CM_STOR_DIFFAMP_GAIN0,CM_STOR_DIFFAMP_GAIN1,CM_STOR_DIFFAMP_N1,CM_STOR_DIFFAMP_OUT,CM_STOR_DIFFAMP_P1,CM_STOR_OPAMP_ENABLE,CM_STOR_OPAMP_N,CM_STOR_OPAMP_OUT,CM_STOR_V_OFFSET_IN,CM_STORV_SENSE_N,CM_STOR_V_SENSE_N,CM_STOR_V_SENSE_P,V_SENSE_P">
+<bus name="POWER_SENSING:CM_DIFFAMP_N4,CM_DIFFAMP_P4,CM_DTR0_DCBIAS_SHUTDOWN,CM_DTR0_DIFFAMP_GAIN0,CM_DTR0_DIFFAMP_GAIN1,CM_DTR0_DIFFAMP_N,CM_DTR0_DIFFAMP_OUT,CM_DTR0_DIFFAMP_P3,CM_DTR0_OPAMP_ENABLE,CM_DTR0_OPAMP_N,CM_DTR0_OPAMP_OUT,CM_DTR0_V_OFFSET_IN,CM_DTR0_V_SENSE_N,CM_DTR0_V_SENSE_P,CM_DTR1_DCBIAS_SHUTDOWN,CM_DTR1_DIFFAMP_GAIN0,CM_DTR1_DIFFAMP_GAIN1,CM_DTR1_DIFFAMP_N,CM_DTR1_DIFFAMP_OUT,CM_DTR1_DIFFAMP_P,CM_DTR1_OPAMP_N,CM_DTR1_OPAMP_OUT,CM_DTR1_OPAMP_P,CM_DTR1_V_OFFSET_IN,CM_DTR1_V_SENSE_N,CM_DTR1_V_SENSE_P,CM_DTR_OPAMP_ENABLE,CM_OPAMP_ENABLE4,CM_OPAMP_N4,CM_OPAMP_OUT4,CM_OPAMP_P1,CM_OPAMP_P3,CM_OPAMP_P4,CM_PROC_DCBIAS_SHUTDOWN,CM_PROC_DIFFAMP_GAIN0,CM_PROC_DIFFAMP_GAIN1,CM_PROC_DIFFAMP_OUT,CM_PROC_V_OFFSET_IN,CM_PROC_V_SENSE_N,CM_PROC_V_SENSE_P,CM_STOR_DCBIAS_SHUTDOWN,CM_STOR_DIFFAMP_GAIN0,CM_STOR_DIFFAMP_GAIN1,CM_STOR_DIFFAMP_N1,CM_STOR_DIFFAMP_OUT,CM_STOR_DIFFAMP_P1,CM_STOR_OPAMP_ENABLE,CM_STOR_OPAMP_N,CM_STOR_OPAMP_OUT,CM_STOR_V_OFFSET_IN,CM_STOR_V_SENSE_N,CM_STOR_V_SENSE_P,V_SENSE_P">
 <segment>
 <wire x1="421.64" y1="223.52" x2="533.4" y2="223.52" width="0.762" layer="92"/>
@@
 </segment>
 </net>
-<net name="CM_STORV_SENSE_N" class="0">
+<net name="CM_STOR_V_SENSE_N" class="0">
 <segment>
 <pinref part="J3" gate="G$1" pin="22"/>
@@
 </instances>
 <busses>
-<bus name="POWER_SENSING:CM_DIFFAMP_N4,CM_DIFFAMP_P4,CM_DTR0_DCBIAS_SHUTDOWN,CM_DTR0_DIFFAMP_GAIN0,CM_DTR0_DIFFAMP_GAIN1,CM_DTR0_DIFFAMP_N,CM_DTR0_DIFFAMP_OUT,CM_DTR0_DIFFAMP_P3,CM_DTR0_OPAMP_ENABLE,CM_DTR0_OPAMP_N,CM_DTR0_OPAMP_OUT,CM_DTR0_V_OFFSET_IN,CM_DTR0_V_SENSE_N,CM_DTR0_V_SENSE_P,CM_DTR1_DCBIAS_SHUTDOWN,CM_DTR1_DIFFAMP_GAIN0,CM_DTR1_DIFFAMP_GAIN1,CM_DTR1_DIFFAMP_N,CM_DTR1_DIFFAMP_OUT,CM_DTR1_DIFFAMP_P,CM_DTR1_OPAMP_N,CM_DTR1_OPAMP_OUT,CM_DTR1_OPAMP_P,CM_DTR1_V_OFFSET_IN,CM_DTR1_V_SENSE_N,CM_DTR1_V_SENSE_P,CM_DTR_OPAMP_ENABLE,CM_OPAMP_ENABLE4,CM_OPAMP_N4,CM_OPAMP_OUT4,CM_OPAMP_P1,CM_OPAMP_P3,CM_OPAMP_P4,CM_PROC_DCBIAS_SHUTDOWN,CM_PROC_DIFFAMP_GAIN0,CM_PROC_DIFFAMP_GAIN1,CM_PROC_DIFFAMP_OUT,CM_PROC_V_OFFSET_IN,CM_PROC_V_SENSE_N,CM_PROC_V_SENSE_P,CM_STOR_DCBIAS_SHUTDOWN,CM_STOR_DIFFAMP_GAIN0,CM_STOR_DIFFAMP_GAIN1,CM_STOR_DIFFAMP_N1,CM_STOR_DIFFAMP_OUT,CM_STOR_DIFFAMP_P1,CM_STOR_OPAMP_ENABLE,CM_STOR_OPAMP_N,CM_STOR_OPAMP_OUT,CM_STOR_V_OFFSET_IN,CM_STORV_SENSE_N,CM_STOR_V_SENSE_N,CM_STOR_V_SENSE_P,V_SENSE_P">
+<bus name="POWER_SENSING:CM_DIFFAMP_N4,CM_DIFFAMP_P4,CM_DTR0_DCBIAS_SHUTDOWN,CM_DTR0_DIFFAMP_GAIN0,CM_DTR0_DIFFAMP_GAIN1,CM_DTR0_DIFFAMP_N,CM_DTR0_DIFFAMP_OUT,CM_DTR0_DIFFAMP_P3,CM_DTR0_OPAMP_ENABLE,CM_DTR0_OPAMP_N,CM_DTR0_OPAMP_OUT,CM_DTR0_V_OFFSET_IN,CM_DTR0_V_SENSE_N,CM_DTR0_V_SENSE_P,CM_DTR1_DCBIAS_SHUTDOWN,CM_DTR1_DIFFAMP_GAIN0,CM_DTR1_DIFFAMP_GAIN1,CM_DTR1_DIFFAMP_N,CM_DTR1_DIFFAMP_OUT,CM_DTR1_DIFFAMP_P,CM_DTR1_OPAMP_N,CM_DTR1_OPAMP_OUT,CM_DTR1_OPAMP_P,CM_DTR1_V_OFFSET_IN,CM_DTR1_V_SENSE_N,CM_DTR1_V_SENSE_P,CM_DTR_OPAMP_ENABLE,CM_OPAMP_ENABLE4,CM_OPAMP_N4,CM_OPAMP_OUT4,CM_OPAMP_P1,CM_OPAMP_P3,CM_OPAMP_P4,CM_PROC_DCBIAS_SHUTDOWN,CM_PROC_DIFFAMP_GAIN0,CM_PROC_DIFFAMP_GAIN1,CM_PROC_DIFFAMP_OUT,CM_PROC_V_OFFSET_IN,CM_PROC_V_SENSE_N,CM_PROC_V_SENSE_P,CM_STOR_DCBIAS_SHUTDOWN,CM_STOR_DIFFAMP_GAIN0,CM_STOR_DIFFAMP_GAIN1,CM_STOR_DIFFAMP_N1,CM_STOR_DIFFAMP_OUT,CM_STOR_DIFFAMP_P1,CM_STOR_OPAMP_ENABLE,CM_STOR_OPAMP_N,CM_STOR_OPAMP_OUT,CM_STOR_V_OFFSET_IN,CM_STOR_V_SENSE_N,CM_STOR_V_SENSE_P,V_SENSE_P">
 <segment>
 <wire x1="15.24" y1="416.56" x2="645.16" y2="416.56" width="0.762" layer="92"/>

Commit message: Minor changes, BOM generation & formatting, CAM for debug
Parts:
- J3: MP (none) -> DF40C-50DP-0.4V(51); MPN (none) -> DF40C-50DP-0.4V(51); PART_NO (none) -> DF40C-50DP-0.4V(51)
- JP1: MP (none) -> TSW-112-07-T-S; MPN (none) -> TSW-112-07-T-S; PART_NO (none) -> TSW-112-07-T-S
- S.ERASE, S.NRST: MP (none) -> RS-187R05A2-DS MT RT; MPN EVQP7L01P -> RS-187R05A2-DS MT RT; PART_NO (none) -> RS-187R05A2-DS MT RT
- U.IP: MP (none) -> ATSAM3X8EAAU; PART_NO (none) -> ATSAM3X8EAAU
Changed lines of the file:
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@@
 <part name="U.IP" library="Processors" deviceset="ATSAM3X8EA" device="AU" value="ATSAM3X8EA-AU">
 <attribute name="MANUFACTURER" value="Atmel"/>
+<attribute name="MP" value="ATSAM3X8EAAU"/>
 <attribute name="MPN" value="ATSAM3X8EAAU"/>
+<attribute name="PART_NO" value="ATSAM3X8EAAU"/>
 </part>
 <part name="GND109" library="Supplies" deviceset="GND" device=""/>
@@
 </part>
 <part name="S.NRST" library="Switches" deviceset="MOMENTARY-SWITCH-SPST" device="-SMD-5.2MM" value="Momentary">
-<attribute name="MPN" value="EVQP7L01P"/>
+<attribute name="MP" value="RS-187R05A2-DS MT RT"/>
+<attribute name="MPN" value="RS-187R05A2-DS MT RT"/>
+<attribute name="PART_NO" value="RS-187R05A2-DS MT RT"/>
 </part>
 <part name="C28" library="Capacitors" deviceset="C-" device="0402" value="10n">
@@
 </part>
 <part name="S.ERASE" library="Switches" deviceset="MOMENTARY-SWITCH-SPST" device="-SMD-5.2MM" value="Momentary">
-<attribute name="MPN" value="EVQP7L01P"/>
+<attribute name="MP" value="RS-187R05A2-DS MT RT"/>
+<attribute name="MPN" value="RS-187R05A2-DS MT RT"/>
+<attribute name="PART_NO" value="RS-187R05A2-DS MT RT"/>
 </part>
 <part name="MN.UART.TX" library="Connectors" deviceset="JUMPER-SMT_2_NC_PASTE" device="_NO-SILK" package3d_urn="urn:adsk.eagle:package:39283/1"/>
@@
 <attribute name="VOLTAGE" value="10V"/>
 </part>
-<part name="J3" library="Connectors" deviceset="HIROSE-DF40_50-PIN_CONNECTORS" device="-HEADER"/>
+<part name="J3" library="Connectors" deviceset="HIROSE-DF40_50-PIN_CONNECTORS" device="-HEADER">
+<attribute name="MP" value="DF40C-50DP-0.4V(51)"/>
+<attribute name="MPN" value="DF40C-50DP-0.4V(51)"/>
+<attribute name="PART_NO" value="DF40C-50DP-0.4V(51)"/>
+</part>
 <part name="LOW_BAT" library="Diodes" deviceset="LED" device="CHIPLED_0603">
 <attribute name="COLOR" value="Orange"/>
@@
 <attribute name="PART_NO" value="ERJ-2GEJ271X"/>
 </part>
-<part name="JP1" library="Connectors" deviceset="J-HEADER-1X12" device=""/>
+<part name="JP1" library="Connectors" deviceset="J-HEADER-1X12" device="">
+<attribute name="MP" value="TSW-112-07-T-S"/>
+<attribute name="MPN" value="TSW-112-07-T-S"/>
+<attribute name="PART_NO" value="TSW-112-07-T-S"/>
+</part>
 <part name="SUPPLY11" library="Supplies" deviceset="+3V3" device=""/>
 <part name="GND6" library="Supplies" deviceset="GND" device=""/>
@@
 <attribute name="NAME" x="215.9" y="93.98" size="1.778" layer="95"/>
 <attribute name="MPN" x="215.9" y="91.44" size="1.778" layer="96"/>
+<attribute name="MP" x="220.98" y="96.52" size="1.778" layer="96" display="off"/>
+<attribute name="PART_NO" x="220.98" y="96.52" size="1.778" layer="96" display="off"/>
 </instance>
 <instance part="GND109" gate="1" x="246.38" y="261.62" smashed="yes"/>
@@
 <attribute name="NAME" x="285.496" y="302.26" size="1.778" layer="95" font="vector" rot="R90" align="bottom-center"/>
 <attribute name="MPN" x="281.94" y="302.26" size="1.778" layer="96" rot="R90" display="off"/>
+<attribute name="MP" x="281.94" y="302.26" size="1.778" layer="96" rot="R90" display="off"/>
+<attribute name="PART_NO" x="281.94" y="302.26" size="1.778" layer="96" rot="R90" display="off"/>
 </instance>
 <instance part="C28" gate="G$1" x="281.94" y="314.96" smashed="yes">
@@
 <attribute name="NAME" x="350.52" y="94.996" size="1.778" layer="95" font="vector" rot="R180" align="bottom-center"/>
 <attribute name="MPN" x="350.52" y="91.44" size="1.778" layer="96" rot="R180" display="off"/>
+<attribute name="MP" x="350.52" y="91.44" size="1.778" layer="96" rot="R180" display="off"/>
+<attribute name="PART_NO" x="350.52" y="91.44" size="1.778" layer="96" rot="R180" display="off"/>
 </instance>
 <instance part="MN.UART.TX" gate="G$1" x="510.54" y="205.74" smashed="yes">
@@
 <instance part="J3" gate="G$1" x="508" y="137.16" smashed="yes" rot="R90">
 <attribute name="NAME" x="474.1966" y="129.51801875" size="1.273659375" layer="95" rot="R90"/>
+<attribute name="MPN" x="508" y="137.16" size="1.778" layer="96" rot="R90" display="off"/>
+<attribute name="MP" x="508" y="137.16" size="1.778" layer="96" rot="R90" display="off"/>
+<attribute name="PART_NO" x="508" y="137.16" size="1.778" layer="96" rot="R90" display="off"/>
 </instance>
 <instance part="LOW_BAT" gate="G$1" x="152.4" y="114.3" smashed="yes">
@@
 <attribute name="NAME" x="427.99" y="43.815" size="1.778" layer="95"/>
 <attribute name="VALUE" x="430.53" y="7.62" size="1.778" layer="96"/>
+<attribute name="MP" x="436.88" y="25.4" size="1.778" layer="96" display="off"/>
+<attribute name="MPN" x="436.88" y="25.4" size="1.778" layer="96" display="off"/>
+<attribute name="PART_NO" x="436.88" y="25.4" size="1.778" layer="96" display="off"/>
 </instance>
 <instance part="SUPPLY11" gate="G$1" x="416.56" y="48.26" smashed="yes"/>
